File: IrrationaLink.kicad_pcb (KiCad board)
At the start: 2 copper layers, 35 x 24 mm, 38 parts, among them J1 USB_C_Receptacle_USB2.0, J2 Conn_02x05_Odd_Even, J3 Conn_02x05_Odd_Even, SW1 SW_Push, U1 ESP32-C3, U2 LM2937xMP, Y1 ABM11W-40.0000MHZ-8-B1U-T3

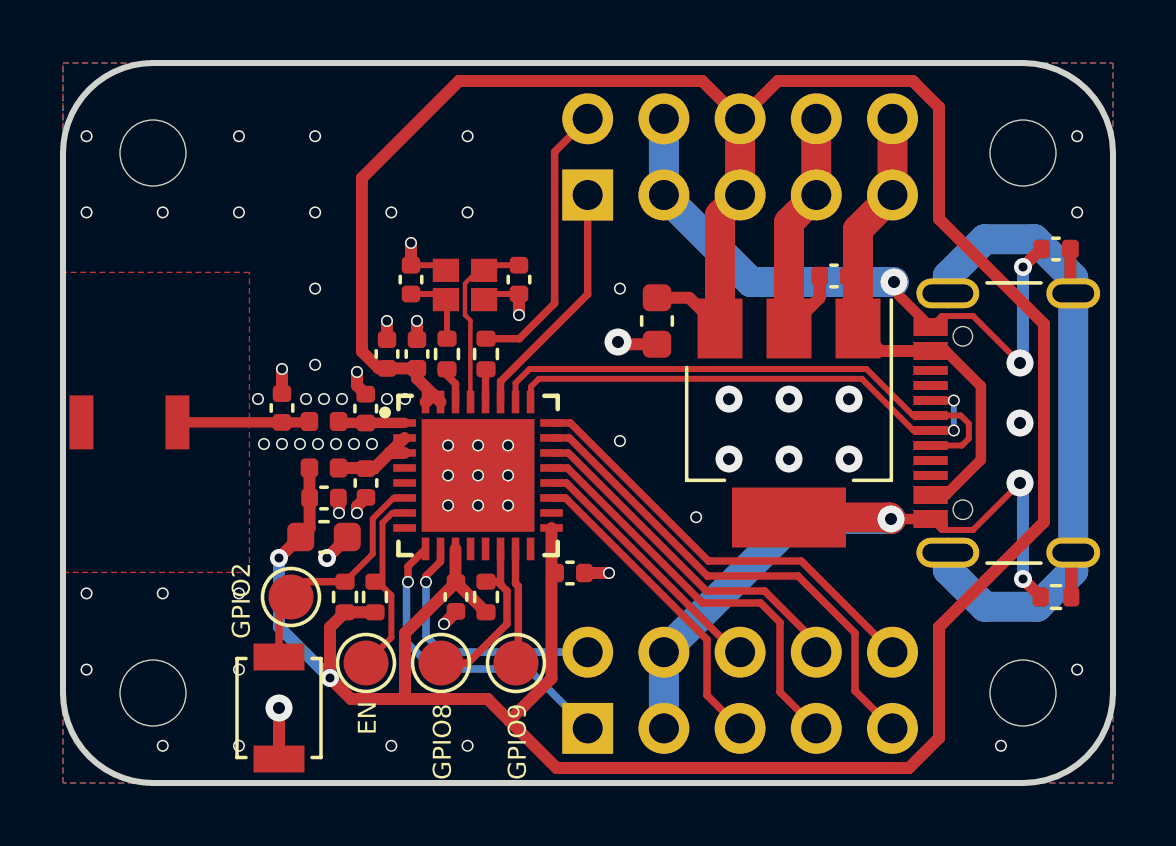
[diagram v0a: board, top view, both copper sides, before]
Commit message: Add USB resistors to PCB
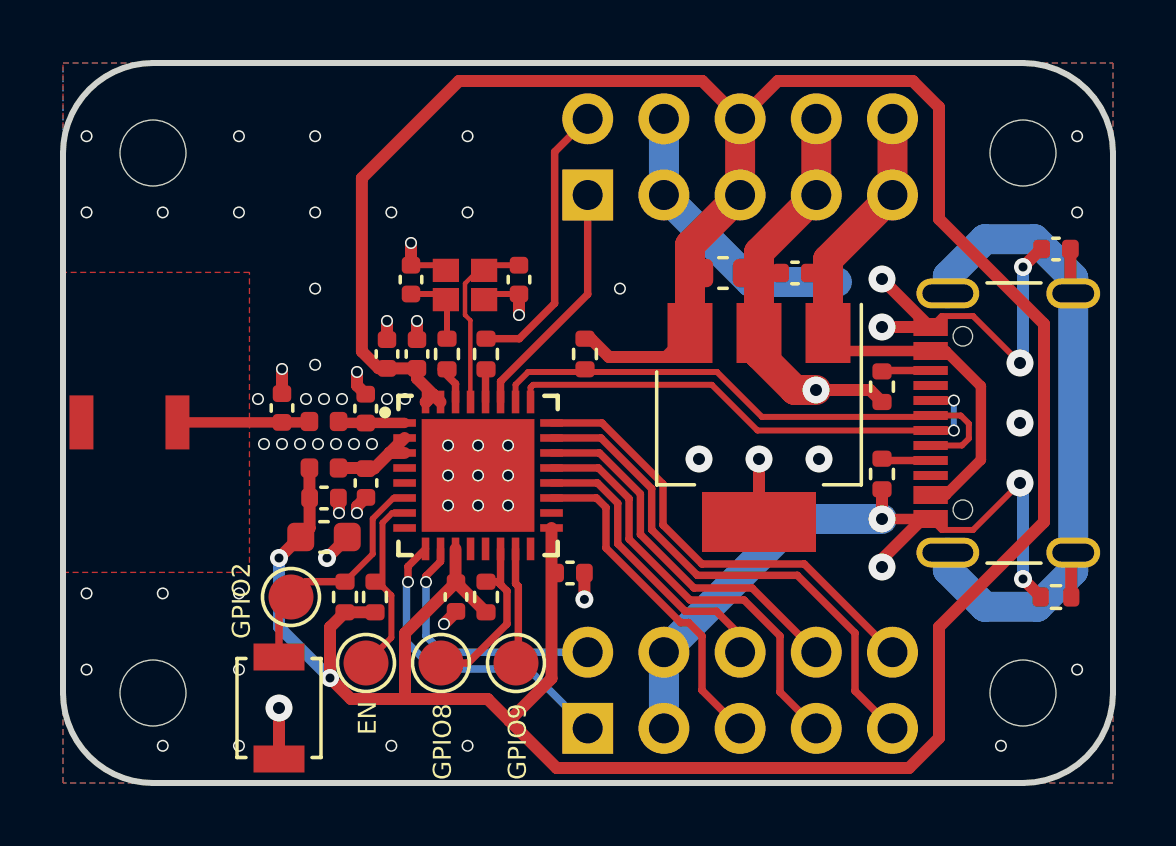
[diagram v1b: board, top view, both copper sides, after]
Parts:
- added R7: 5k1, Resistor_SMD:R_0402_1005Metric, F.Cu at (146.3, 80.8)
- added R8: 5k1, Resistor_SMD:R_0402_1005Metric, F.Cu at (146.3, 83.7)
- added R9: 1k5, Resistor_SMD:R_0402_1005Metric, F.Cu at (136.4, 79.7)
- moved C13 2.72 mm to (141.0, 77.0), turned to 0 degrees
- moved C12 1.30 mm to (143.4, 77.0)
- moved U2 1.01 mm to (142.2, 82.2)
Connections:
- J1 pad A5: unconnected-(J1-CC1-PadA5) -> /CC1
- J1 pad B5: unconnected-(J1-CC2-PadB5) -> /CC2
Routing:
- net GND: track 68.8 -> 74.6 mm, vias 76 -> 73
- net +3V3: track 113.0 -> 115.1 mm
- net /CC1: track 0.00 -> 1.64 mm
- net /CC2: track 0.00 -> 1.63 mm
- net VBUS: track 17.0 -> 18.5 mm
- net /GPIO13: track 8.62 -> 9.75 mm
- net /GPIO17: track 14.5 -> 15.3 mm
- net /GPIO16: track 16.5 -> 17.3 mm
- net /GPIO12: track 10.6 -> 11.3 mm
- net /GPIO15: track 11.8 -> 12.4 mm
- net /GPIO14: track 13.8 -> 14.3 mm
